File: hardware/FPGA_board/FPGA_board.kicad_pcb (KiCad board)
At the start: 6 copper layers, 50.9 x 24.8 mm, 142 parts, among them J1 USB_C_Receptacle_USB2.0, J2 Conn_01x6_Male, J3 USB_C_Receptacle_USB2.0, J4 MicroSd, J5 Conn_01x03, J6 JTAG, J7 Conn_02x15_Odd_Even, J8 Conn_02x15_Odd_Even, SW1 SW_Push, U1 RY1303 or EA3036, U10 NCP115-2.5, U3 ECP5U25, U4 MT41K64M16TW-107_J-TR, U6 XT25Q08DDTIGT, U8 TPS51206

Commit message: update PCB design files
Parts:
- added G***: LOGO, LOGO, B.Cu at (176.1, 92.9)
- added G***: LOGO, LOGO, B.Cu at (162.9, 93.3)

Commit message: update PCB design files
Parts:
- removed the G*** at (176.1, 92.9)
- removed the G*** at (162.9, 93.3)
- removed H4: MountingHole, MountingHole:MountingHole_2.1mm
- removed J1, J3: USB_C_Receptacle_USB2.0, Connector_USB:USB_C_Receptacle_G-Switch_GT-USB-7010ASV
- removed TP19, TP20: SMD_TP, gkl_misc:TestPoint_Pad_D0.5mm
- removed TP3, TP4: , 
- removed U10: NCP115-2.5, gkl_housings_son:X2SON_4_1.0x1.0mm
- added C13: 100pF, Capacitor_SMD:C_0201_0603Metric, F.Cu at (164.8, 109.8)
- added C28: 4.7uF, Capacitor_SMD:C_0402_1005Metric, F.Cu at (170.8, 111.7)
- added C29: 100nF, Capacitor_SMD:C_0201_0603Metric, B.Cu at (157.7, 110.9)
- added D2: D_Schottky, Library:U-DFN1608-2_L1.6-W0.8-RD, F.Cu at (149.5, 94.1)
- added G***: LOGO, LOGO, B.Cu at (171.0, 104.0)
- added G***: LOGO, LOGO, B.Cu at (182.6, 109.8)
- added J10: Conn_01x04, Connector_PinHeader_2.54mm:PinHeader_1x04_P2.54mm_Vertical, B.Cu at (155.5, 91.5)
- added J9: TF TF-018 1.5mm, Library:TF-SMD_TF-018, B.Cu at (149.7, 103.6)
- added JP1: SolderJumper_3_Bridged12, Jumper:SolderJumper-3_P1.3mm_Bridged12_RoundedPad1.0x1.5mm, B.Cu at (148.5, 93.7)
- added JP2: SolderJumper_3_Bridged12, Jumper:SolderJumper-3_P1.3mm_Bridged12_RoundedPad1.0x1.5mm, B.Cu at (166.7, 110.1)
- added JP3: SolderJumper_2_Open, Jumper:SolderJumper-2_P1.3mm_Open_RoundedPad1.0x1.5mm, B.Cu at (181.4, 107.3)
- added L1: 2.2uH, Library:Murata_DFE201612P-2R2M=P2, F.Cu at (149.0, 105.2)
- added L2: 2.2uH, Library:Murata_DFE201612P-2R2M=P2, F.Cu at (153.2, 98.2)
- added L3: 2.2uH, Library:Murata_DFE201612P-2R2M=P2, F.Cu at (153.4, 106.1)
- added L4: 2.2uH, Library:Murata_DFE201612P-2R2M=P2, F.Cu at (166.7, 110.9)
- added R31: 22, Resistor_SMD:R_0402_1005Metric, F.Cu at (188.9, 103.6)
- added R32: 22, Resistor_SMD:R_0402_1005Metric, F.Cu at (187.9, 103.6)
- added R33: 15k, Resistor_SMD:R_0201_0603Metric, F.Cu at (162.8, 109.8)
- added R34: 4.7k, Resistor_SMD:R_0201_0603Metric, F.Cu at (162.5, 108.7)
- added R35: 15, Resistor_SMD:R_0201_0603Metric, B.Cu at (161.6, 110.5)
- added R36: 15, Resistor_SMD:R_0201_0603Metric, B.Cu at (158.7, 110.5)
- added R37: 75, Resistor_SMD:R_0201_0603Metric, B.Cu at (160.1, 110.5)
- added R38: 15, Resistor_SMD:R_0201_0603Metric, B.Cu at (161.6, 111.2)
- added R39: 15, Resistor_SMD:R_0201_0603Metric, B.Cu at (158.7, 111.2)
- added TP1: SMD_TP, TestPoint:TestPoint_Pad_D1.0mm, B.Cu at (143.4, 112.0)
- added TP2: SMD_TP, TestPoint:TestPoint_Pad_D1.0mm, B.Cu at (143.4, 109.9)
- added U2: TLV62569APDRL, Package_TO_SOT_SMD:SOT-563, F.Cu at (164.1, 111.3)
- added U5: Si5351A-B-GT, Package_SO:MSOP-10_3x3mm_P0.5mm, B.Cu at (160.3, 108.3)
- added U7: NCP115AMX250TCG, Package_DFN_QFN:OnSemi_XDFN4-1EP_1.0x1.0mm_EP0.52x0.52mm, F.Cu at (168.8, 111.5)
- added USBD1: USB_C_Receptacle_USB2.0, Connector_USB:USB_C_Receptacle_G-Switch_GT-USB-7010ASV, F.Cu at (142.3, 95.6)
- added USBH1: USB_C_Receptacle_USB2.0, Connector_USB:USB_C_Receptacle_G-Switch_GT-USB-7010ASV, F.Cu at (142.4, 110.3)
- added Y1: 27MHz, Crystal:Crystal_SMD_2016-4Pin_2.0x1.6mm, B.Cu at (155.7, 110.3)
- C70, C71, FB1: moved to F.Cu
- J2, J5, R26, R30: moved to B.Cu
- J4: value MicroSd -> Conn_01x04_Male; footprint Connector_Card:microSD_HC_Molex_104031-0811 -> Connector_PinHeader_2.54mm:PinHeader_1x04_P2.54mm_Vertical
- J7, J8: footprint gkl_conn:DF12(3.0)-30DP-0.5V(86) -> Library:DF12NB3030DP05V51
- R10, R9: value 51K -> 12K
- R15: value 120K -> 120K 1%; footprint Resistor_SMD:R_0201_0603Metric -> Resistor_SMD:R_0402_1005Metric
- R16: value 82K -> 82K 1%; footprint Resistor_SMD:R_0201_0603Metric -> Resistor_SMD:R_0402_1005Metric
- R17, R18, R5: value 100k -> 100k 1%
- R2: value 22K -> 22K 1%; footprint Resistor_SMD:R_0201_0603Metric -> Resistor_SMD:R_0402_1005Metric
- R29: footprint Resistor_SMD:R_0201_0603Metric -> Resistor_SMD:R_0402_1005Metric
- SW1: footprint gkl_misc:PTS_810_SMT_Switch -> Button_Switch_SMD:SW_SPST_PTS810
- TP26, TP27: footprint gkl_misc:TestPoint_Pad_D0.5mm -> TestPoint:TestPoint_Pad_D1.0mm
- TP28, TP29, TP30, TP31, TP32, TP33: footprint gkl_misc:TestPoint_Pad_D0.5mm -> Library:TestPoint_Pad_D0.5mm
- U3: value ECP5U25 -> ECP5
- U6: value XT25Q08DDTIGT -> W25Q128JVPIQ; footprint gkl_housings_dfn:DFN-8-1EP_3x2mm_Pitch0.5mm -> Package_SON:WSON-8-1EP_6x5mm_P1.27mm_EP3.4x4.3mm
- moved J4 31.6 mm to (178.4, 91.5), turned to 90 degrees
- moved TP32 15.4 mm to (147.6, 109.7), turned to 180 degrees
- moved R28 14.8 mm to (146.1, 108.2), turned to 0 degrees
- moved TP29 14.0 mm to (141.1, 102.0), turned to 180 degrees
- moved R30 12.7 mm to (183.4, 99.2)
- moved FB1 11.4 mm to (143.1, 102.2)
- moved R29 11.4 mm to (184.2, 109.8)
- moved RN7 10.9 mm to (145.4, 103.0), turned to 180 degrees
- moved C71 10.6 mm to (144.4, 102.8)
- moved TP31 10.1 mm to (160.2, 103.8), turned to 180 degrees
- moved R26 9.58 mm to (182.5, 95.3), turned to -90 degrees
- moved C47 8.93 mm to (165.9, 108.2), turned to 90 degrees
- moved C3 8.01 mm to (146.0, 102.8), turned to 90 degrees
- moved C70 7.55 mm to (142.9, 103.9), turned to 0 degrees
- moved R14 6.06 mm to (153.1, 95.6)
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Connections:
- net USB_PULLUP renamed PULLUP_USB
- C11 pad 1: GND -> VTT
- C11 pad 2: VTT -> GND
- C14 pad 2: PUSB_VBUS -> VSYS
- C17 pad 1: GND -> P1.1V
- C17 pad 2: P1.1V -> GND
- C18 pad 1: GND -> P1.35V
- C18 pad 2: P1.35V -> GND
- C2 pad 2: PUSB_VBUS -> VSYS
- C3 pad 2: PUSB_VBUS -> VSYS
- C47 pad 1: P2.5V -> Net-(JP2-B)
- C5 pad 2: PUSB_VBUS -> VSYS
- C7 pad 1: GND -> P3.3V
- C7 pad 2: P3.3V -> GND
- C70 pad 2: Net-(J4-Pin_4) -> /sheetSDMMC/VDD_SD
- C71 pad 1: Net-(J4-Pin_4) -> /sheetSDMMC/VDD_SD
- FB1 pad 1: Net-(J4-Pin_4) -> /sheetSDMMC/VDD_SD
- J2 pad 1: IO_1 -> IO_MISO
- J2 pad 2: IO_0 -> IO_1
- J2 pad 3: IO_MISO -> IO_0
- J4 pad 1: SD0_DAT2 -> IO_10
- J4 pad 2: SD0_DAT3 -> IO_9
- J4 pad 3: SD0_CMD -> IO_SCK
- J4 pad 4: Net-(J4-Pin_4) -> IO_13
- J5 pad 1: IO_SDA -> IO_SCL
- J5 pad 2: IO_SCL -> IO_SDA
- J7 pad 1: GND -> IO_11
- J7 pad 10: AUX_1- -> IO_11
- J7 pad 11: AUX_4+ -> LED_B
- J7 pad 12: AUX_1+ -> IO_12
- J7 pad 13: GND -> IO_6
- J7 pad 15: AUX_5- -> IO_SDA
- J7 pad 16: AUX_2- -> IO_9
- J7 pad 17: AUX_5+ -> IO_SCL
- J7 pad 18: AUX_2+ -> IO_10
- J7 pad 19: GND -> IO_5
- J7 pad 21: HPD/ID -> Net-(J7-Pin_21)
- J7 pad 22: AUX_6+ -> IO_5
- J7 pad 24: AUX_6- -> IO_6
- J7 pad 28: LED_G -> Net-(J7-Pin_28)
- J7 pad 3: AUX_3- -> IO_SCK
- J7 pad 30: LED_R -> Net-(J7-Pin_30)
- J7 pad 4: AUX_0- -> AUX_3-
- J7 pad 5: AUX_3+ -> IO_13
- J7 pad 6: AUX_0+ -> AUX_3+
- J7 pad 7: GND -> IO_12
- J7 pad 9: AUX_4- -> Net-(J7-Pin_9)
- J7 pad MP: (no net) -> GND
- J8 pad 10: IO_11 -> AUX_1-
- J8 pad 11: LED_B -> SPI_1
- J8 pad 12: IO_12 -> AUX_1+
- J8 pad 15: IO_SDA -> AUX_5-
- J8 pad 16: IO_9 -> AUX_2-
- J8 pad 17: IO_SCL -> AUX_5+
- J8 pad 18: IO_10 -> AUX_2+
- J8 pad 21: Net-(J8-Pin_21) -> HPD/ID
- J8 pad 22: IO_5 -> AUX_6+
- J8 pad 24: IO_6 -> AUX_6-
- J8 pad 3: SPI_0 -> AUX_4-
- J8 pad 4: IO_SCK -> AUX_0-
- J8 pad 5: SPI_1 -> AUX_4+
- J8 pad 6: IO_13 -> AUX_0+
- J8 pad 9: Net-(J8-Pin_9) -> SPI_0
- J8 pad MP: (no net) -> GND
- R10 pad 1: Net-(J3-CC2) -> P3.3V
- R10 pad 2: GND -> Net-(USBH1-CC2)
- R22 pad 1: LED_R -> LED_G
- R23 pad 1: LED_G -> LED_R
- R26 pad 1: Net-(J8-Pin_9) -> Net-(J7-Pin_9)
- R28 pad 1: P3.3V -> /sheetSDMMC/VDD_SD
- R30 pad 1: Net-(J8-Pin_21) -> Net-(J7-Pin_21)
- R9 pad 1: Net-(J3-CC1) -> P3.3V
- R9 pad 2: GND -> Net-(USBH1-CC1)
- RN7 pad 1: SD0_DAT1 -> SD0_DAT2
- RN7 pad 2: SD0_DAT0 -> SD0_CMD
- RN7 pad 3: SD0_CMD -> SD0_DAT0
- RN7 pad 4: SD0_DAT2 -> SD0_DAT1
- RN7 pad 5: P3.3V -> /sheetSDMMC/VDD_SD
- RN7 pad 6: P3.3V -> /sheetSDMMC/VDD_SD
- RN7 pad 7: P3.3V -> /sheetSDMMC/VDD_SD
- RN7 pad 8: P3.3V -> /sheetSDMMC/VDD_SD
- U1 pad 16: PUSB_VBUS -> VSYS
- U1 pad 19: PUSB_VBUS -> VSYS
- U1 pad 7: PUSB_VBUS -> VSYS
- U4 pad G8: (no net) -> GND
- U4 pad J1: (no net) -> unconnected-(U4-PadJ1)
- U4 pad J9: (no net) -> unconnected-(U4-PadJ9)
- U4 pad L1: (no net) -> unconnected-(U4-PadL1)
- U4 pad L9: (no net) -> unconnected-(U4-PadL9)
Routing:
- net P3.3V: track 174.3 -> 241.5 mm, vias 22 -> 21
- net LED_G: track 80.7 -> 22.8 mm, vias 4 -> 3
- net LED_R: track 74.8 -> 18.7 mm, vias 3 -> 2
- net FPGA_RESET: track 41.1 -> 90.9 mm
- net VSYS: track 0.00 -> 44.7 mm, vias 0 -> 6
- net /sheetHyperRAM/RAM_VDD: track 18.1 -> 60.0 mm, vias 12 -> 11
- net IO_SDA: track 44.1 -> 73.9 mm, vias 3 -> 4
- net AUX_2+: track 30.2 -> 57.3 mm, vias 1 -> 3
- net IO_SCL: track 47.5 -> 73.6 mm, vias 3 -> 4
- net AUX_4+: track 30.6 -> 55.5 mm, vias 1 -> 3
- net AUX_4-: track 30.1 -> 54.9 mm, vias 1 -> 3
- net AUX_2-: track 31.7 -> 55.4 mm, vias 1 -> 3
- net /sheetPower/PGOOD_P1.1V: track 16.5 -> 38.3 mm, vias 2 -> 3
- net /sheetHyperRAM/RAM_VDDQ: track 15.6 -> 36.4 mm
- net AUX_1-: track 34.4 -> 54.9 mm
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- added copper zone on In2.Cu, net (none)
- added copper zone on B.Cu, net GND
- added copper zone on F.Cu, net GND
- added copper zone on F.Cu, net P1.35V
- added copper zone on In1.Cu, net P1.35V
- added copper zone on In2.Cu, net P2.5V
- added copper zone on In2.Cu, net P3.3V
- added copper zone on In1.Cu, net PUSB_VBUS
- added copper zone on In3.Cu, net VSYS
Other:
- board size 50.9 x 24.8 mm -> 51.2 x 25.8 mm
- board text added: "0.275/.15 via handles 1.6A .53/.25 via handles 2.2A .5 track (external) handles 1.4A .2 track (external) handles .73A internal tracks: 5x"
- board text added: "90ohm JLC06161H-3313A coplanar -trace spacing/clearance: .2032mm width: .1554mm"
- board text added: "Avaota-A1 design BGA pad: 0.2285 track: 0.076 clearance: 0.09775 via-in-pad: 0.4/0.3 ovals: 0.2-0.305 (replacing .25) Soldermask: matches BGA pad"
- board text added: "DEV"
- board text added: "FPGA board"
- board text added: "G"
- board text added: "HOST"
- board text added: "Hole to pad distance should be made greater (.18 to .22-.25)"
- board text added: "PCB3D_BR_FPGA_board"
- board text added: "PCB3D_TL_FPGA_board"
- board text added: "RESET"
- board text added: "The design is according to: https://jlcpcb.com/help/article/243-BGA-Design-Guidelines---PCB-Layout-Recommendations-for-BGA-packages That means: 0.25mm BGA pad and Via-In-Pad outer diameter 0.15mm Via holes 0.09mm Minimum for normal tracks 0.076mm Tracks passing between BGA pads (infrequent)"
- board text added: "VBUS"
- board text removed: "+"
- board text removed: "Micro SD"
- board text removed: "Reset"

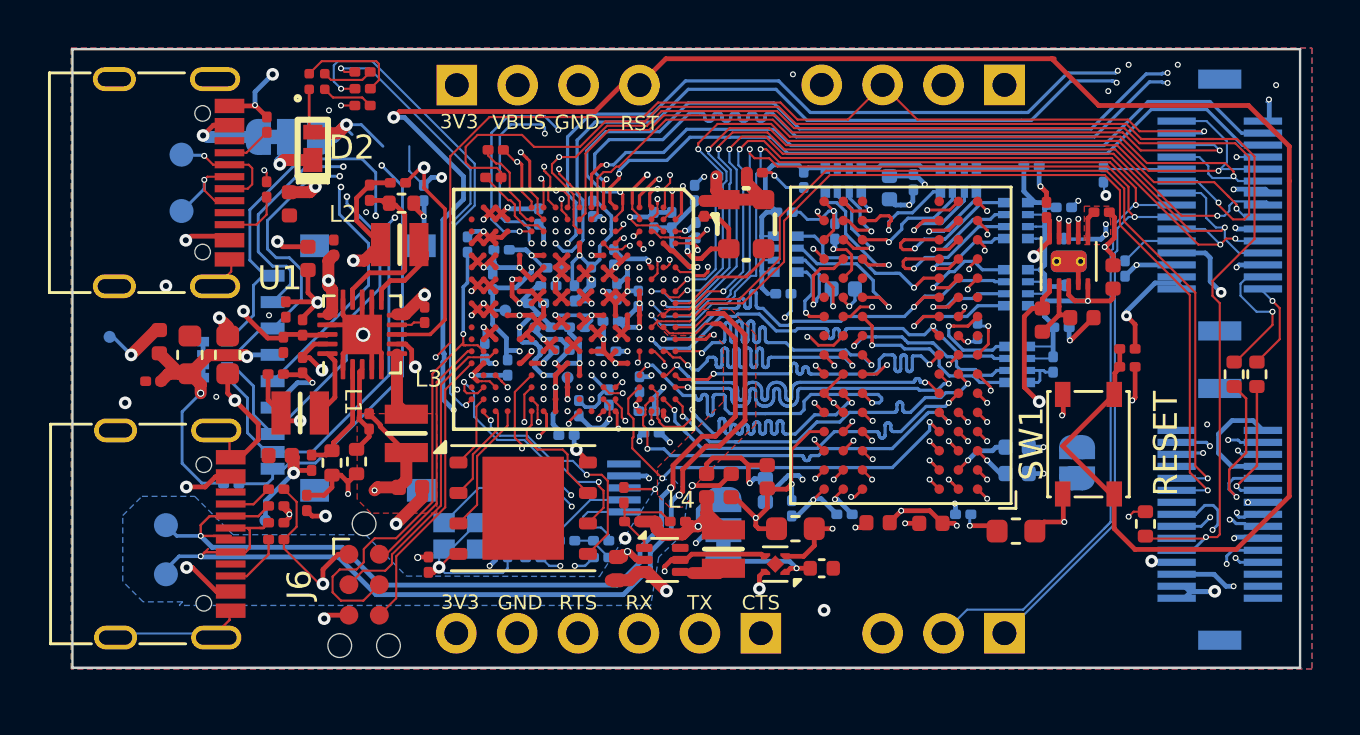
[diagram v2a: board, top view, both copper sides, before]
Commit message: Add documentation regarding DFM analysis and corresponding changes to the 6-layer board design
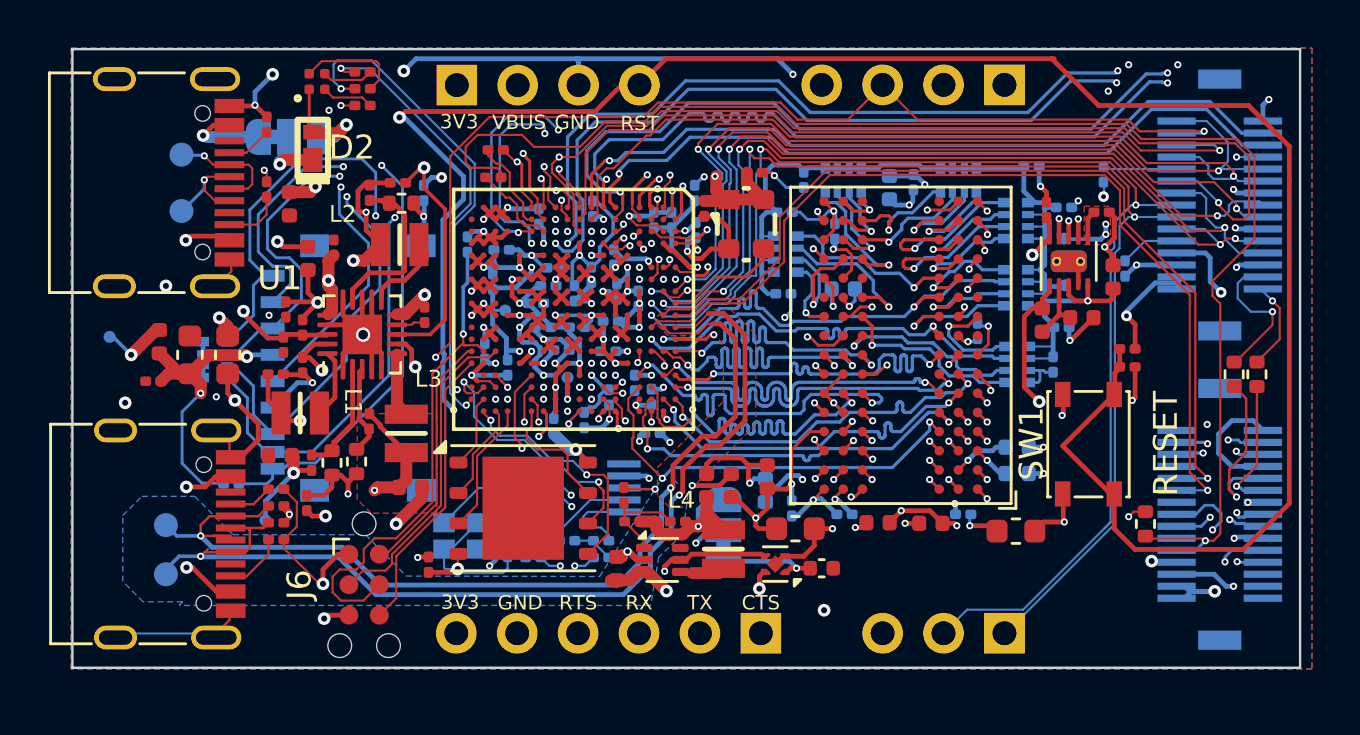
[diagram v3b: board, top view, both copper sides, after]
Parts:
- removed JP3: SolderJumper_2_Open, Jumper:SolderJumper-2_P1.3mm_Open_RoundedPad1.0x1.5mm
- moved G*** 29.0 mm to (157.7, 94.8), turned to 180 degrees
- moved C69 0.65 mm to (159.6, 105.8), turned to 90 degrees
- moved C64 0.63 mm to (163.7, 104.5), turned to 90 degrees
- moved C25 0.54 mm to (160.8, 105.5)
- moved C19 0.21 mm to (162.9, 104.0)
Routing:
- net GND: track 251.5 -> 268.3 mm
- net P1.35V: track 104.1 -> 102.4 mm
- net P3.3V: track 241.5 -> 240.0 mm, vias 21 -> 20
- added copper zone on In2.Cu, net GND
- removed copper zone on In2.Cu, net (none)
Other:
- rule pad_to_mask_clearance: 0.03 -> 0
